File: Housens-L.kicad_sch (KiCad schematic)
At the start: 37 parts, among them J1 JTAG/SWD, J2 USB_C_2.0, SW1 RESET, U1 MCP1603, U2 BME280, U3 OPT3005, U4 STM32WB55CGUx, Y1 32MHz, Y2 32.768kHz

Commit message: Layout antenna
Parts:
- removed D1: D, Diode_SMD:D_0603_1608Metric, symbol Device:D
- added D1: D_Schottky, Diode_SMD:D_0603_1608Metric, symbol Device:D_Schottky
- Y1, Y2: footprint (none) -> Crystal:Crystal_SMD_2520-4Pin_2.5x2.0mm
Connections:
- net +BATT: now also D1.1 (K)
- net CELL: now also D1.2 (A)
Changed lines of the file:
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@@
+	)
+	(symbol
+		(lib_id "Device:D_Schottky")
+		(at 40.64 170.18 180)
+		(unit 1)
+		(exclude_from_sim no)
+		(in_bom yes)
+		(on_board yes)
+		(dnp no)
+		(fields_autoplaced yes)
+		(property "Reference" "D1"
+			(at 40.9575 163.83 0)
+			(effects
+				(font
+					(size 1.27 1.27)
+				)
+			)
+		)
+		(property "Value" "D_Schottky"
+			(at 40.9575 166.37 0)
+			(effects
+				(font
+					(size 1.27 1.27)
+				)
+			)
+		)
+		(property "Footprint" "Diode_SMD:D_0603_1608Metric"
+			(at 40.64 170.18 0)
+			(effects
+				(font
+					(size 1.27 1.27)
+				)
+				(hide yes)
+			)
+		)
+		(property "Datasheet" "~"
+			(at 40.64 170.18 0)
+			(effects
+				(font
+					(size 1.27 1.27)
+				)
+				(hide yes)
+			)
+		)
+		(property "Description" "Schottky diode"
+			(at 40.64 170.18 0)
+			(effects
+				(font
+					(size 1.27 1.27)
+				)
+				(hide yes)
+			)
+		)
+		(pin "2"
+		)
+		(pin "1"
+		)
+		(instances
+			(project ""
+				(path "/36bb4837-104c-4aa4-b300-0e6d0ff24db5"
+					(reference "D1")
+					(unit 1)
+				)
+			)
+		)
 	)
 	(symbol
@@
 	)
 	(symbol
-		(lib_id "Device:D")
-		(at 40.64 170.18 180)
-		(unit 1)
-		(exclude_from_sim no)
-		(in_bom yes)
-		(on_board yes)
-		(dnp no)
-		(fields_autoplaced yes)
-		(property "Reference" "D1"
-			(at 40.64 163.83 0)
-			(effects
-				(font
-					(size 1.27 1.27)
-				)
-			)
-		)
-		(property "Value" "D"
-			(at 40.64 166.37 0)
-			(effects
-				(font
-					(size 1.27 1.27)
-				)
-			)
-		)
-		(property "Footprint" "Diode_SMD:D_0603_1608Metric"
-			(at 40.64 170.18 0)
-			(effects
-				(font
-					(size 1.27 1.27)
-				)
-				(hide yes)
-			)
-		)
-		(property "Datasheet" "~"
-			(at 40.64 170.18 0)
-			(effects
-				(font
-					(size 1.27 1.27)
-				)
-				(hide yes)
-			)
-		)
-		(property "Description" "Diode"
-			(at 40.64 170.18 0)
-			(effects
-				(font
-					(size 1.27 1.27)
-				)
-				(hide yes)
-			)
-		)
-		(property "Sim.Device" "D"
-			(at 40.64 170.18 0)
-			(effects
-				(font
-					(size 1.27 1.27)
-				)
-				(hide yes)
-			)
-		)
-		(property "Sim.Pins" "1=K 2=A"
-			(at 40.64 170.18 0)
-			(effects
-				(font
-					(size 1.27 1.27)
-				)
-				(hide yes)
-			)
-		)
-		(pin "1"
-		)
-		(pin "2"
-		)
-		(instances
-			(project ""
-				(path "/36bb4837-104c-4aa4-b300-0e6d0ff24db5"
-					(reference "D1")
-					(unit 1)
-				)
-			)
-		)
-	)
-	(symbol
 		(lib_id "Device:C")
 		(at 38.1 133.35 0)
@@
 			)
 		)
-		(property "Footprint" ""
+		(property "Footprint" "Crystal:Crystal_SMD_2520-4Pin_2.5x2.0mm"
 			(at 24.13 82.55 0)
 			(effects
@@
 			)
 		)
-		(property "Footprint" ""
+		(property "Footprint" "Crystal:Crystal_SMD_2520-4Pin_2.5x2.0mm"
 			(at 24.13 54.61 0)
 			(effects

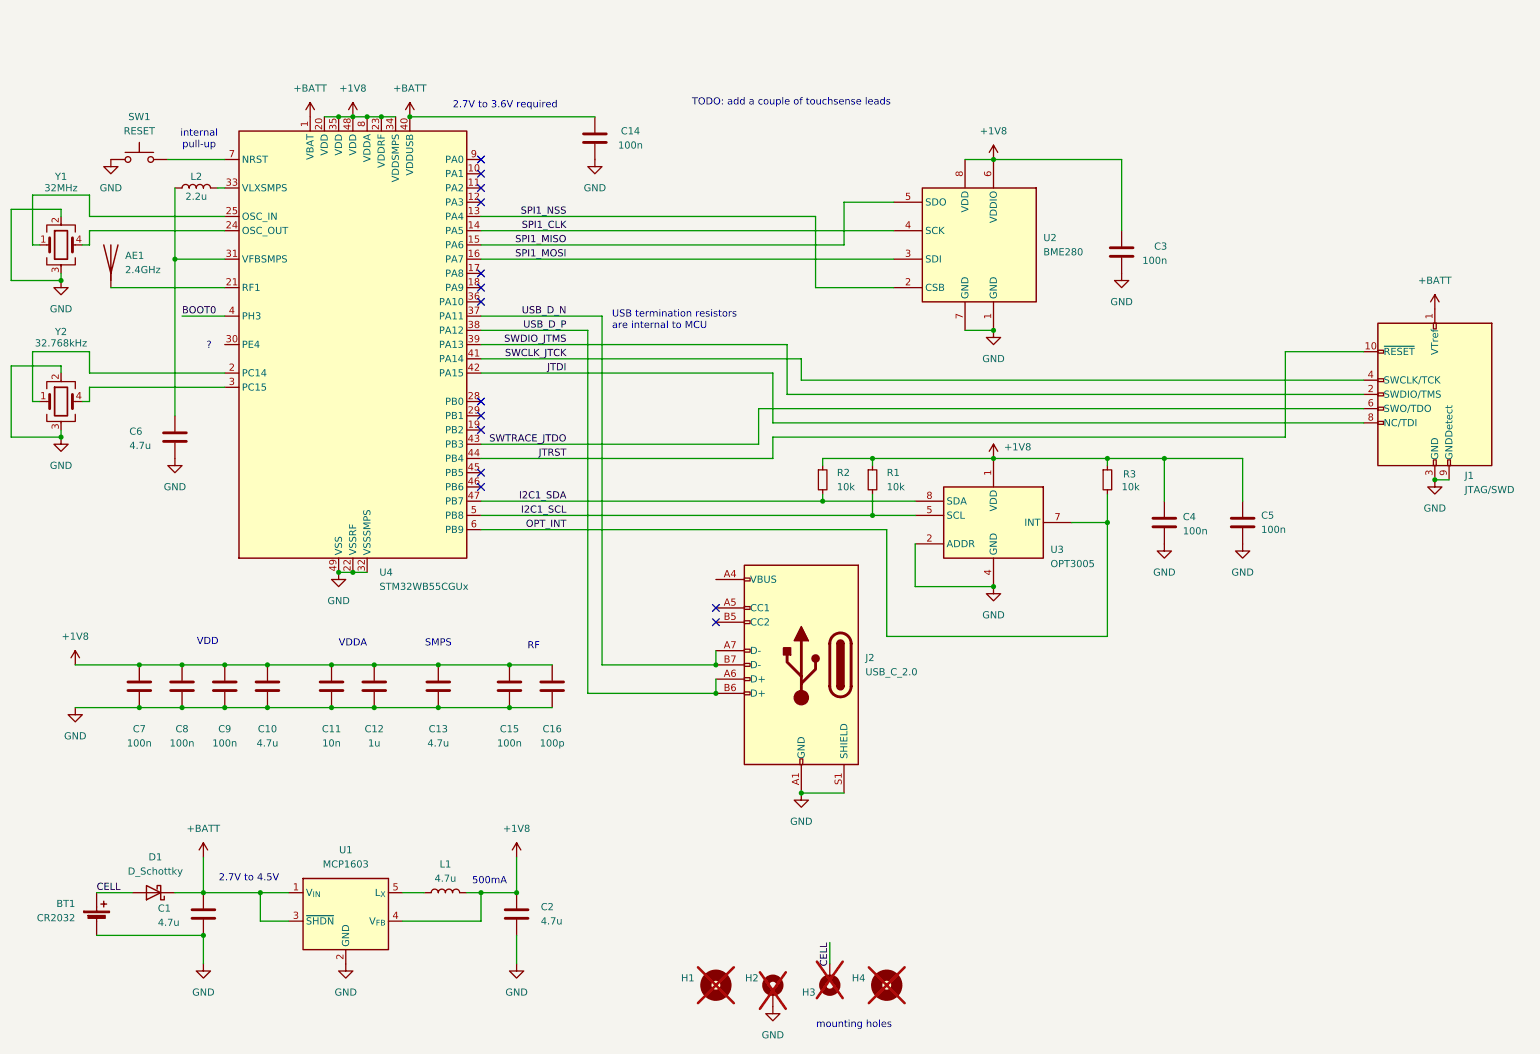
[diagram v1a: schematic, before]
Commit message: Add fuel gauge
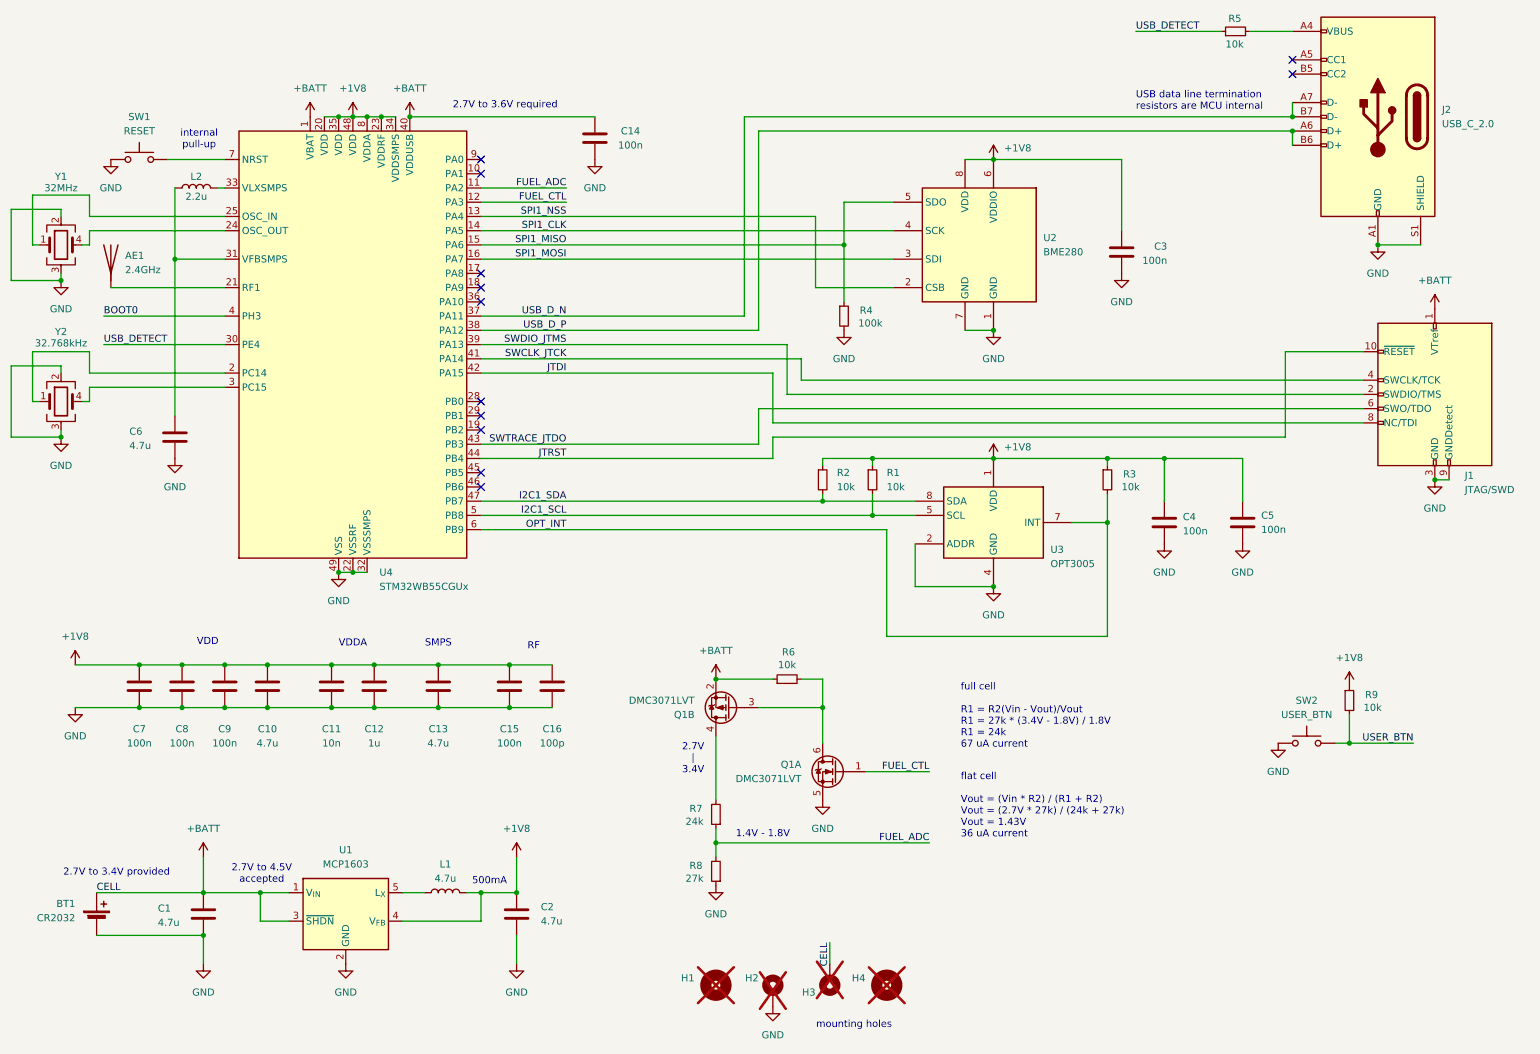
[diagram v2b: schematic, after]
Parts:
- removed D1: D_Schottky, Diode_SMD:D_0603_1608Metric, symbol Device:D_Schottky
- added Q1: DMC3071LVT, Package_TO_SOT_SMD:TSOT-23-6, symbol Transistor_FET:DMC3071LVT
- added R4: 100k, Resistor_SMD:R_0603_1608Metric, symbol Device:R_Small
- added R5, R6, R9: 10k, Resistor_SMD:R_0603_1608Metric, symbol Device:R_Small
- added R7: 24k, Resistor_SMD:R_0603_1608Metric, symbol Device:R_Small
- added R8: 27k, Resistor_SMD:R_0603_1608Metric, symbol Device:R_Small
- added SW2: USER_BTN, Button_Switch_THT:SW_PUSH_6mm, symbol Switch:SW_Push
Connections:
- net CELL is gone; now on net +BATT: BT1.1 (+), H3.1
- net +1V8: now also R9.1
- net +BATT: now also Q1.2 (S), R6.1
- net GND: now also Q1.5 (S), R4.2, R8.1, SW2.1
- net SPI1_MISO: now also R4.1
- net FUEL_ADC: now reaches U4.11 (PA2)
- net FUEL_ADC: now also R7.1, R8.2
- net FUEL_CTL: now reaches U4.12 (PA3)
- net FUEL_CTL: now also Q1.1 (G)
- net USB_DETECT: now reaches U4.30 (PE4)
- net USB_DETECT: now also R5.1
- net at J2.A4 (VBUS), J2.A9 (VBUS), J2.B4 (VBUS)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: now also R5.2
- new net: Q1.3 (G), Q1.6 (D), R6.2
- new net: Q1.4 (D), R7.2
- new net USER_BTN: R9.2, SW2.2
- no-connect marks 14 -> 12
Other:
- note added: "1.4V - 1.8V"
- note added: "2.7V to 3.4V provided"
- note added: "2.7V to 4.5V accepted"
- note added: "2.7V | 3.4V"
- note added: "USB data line termination resistors are MCU internal"
- note added: "flat cell Vout = (Vin * R2) / (R1 + R2) Vout = (2.7V * 27k) / (24k + 27k) Vout = 1.43V 36 uA current"
- note added: "full cell R1 = R2(Vin - Vout)/Vout R1 = 27k * (3.4V - 1.8V) / 1.8V R1 = 24k 67 uA current"
- note removed: "2.7V to 4.5V"
- note removed: "?"
- note removed: "TODO: add a couple of touchsense leads"
- note removed: "USB termination resistors are internal to MCU"
- moved on the sheet: J2

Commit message: Custom thermal footprint for MCU
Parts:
- U4: footprint Package_DFN_QFN:QFN-48-1EP_7x7mm_P0.5mm_EP5.6x5.6mm -> Invented:QFN-48-1EP_7x7mm_P0.5mm_EP5.6x5.6mm_ThermalVias_OneSided
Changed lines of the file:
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@@
 			)
 		)
-		(property "Footprint" "Package_DFN_QFN:QFN-48-1EP_7x7mm_P0.5mm_EP5.6x5.6mm"
+		(property "Footprint" "Invented:QFN-48-1EP_7x7mm_P0.5mm_EP5.6x5.6mm_ThermalVias_OneSided"
 			(at 55.88 110.49 0)
 			(effects
